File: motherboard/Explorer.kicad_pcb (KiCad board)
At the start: 2 copper layers, 80 x 55 mm, 73 parts, among them J1 USB_B, J2 EHZ, J3 EHN, J4 TTL_DEBUG, J5 MODE_SEL, J6 EHE, SW1 RESET, U1 ADS1262IPWR, U2 AMS1117-3.3, U4 locked

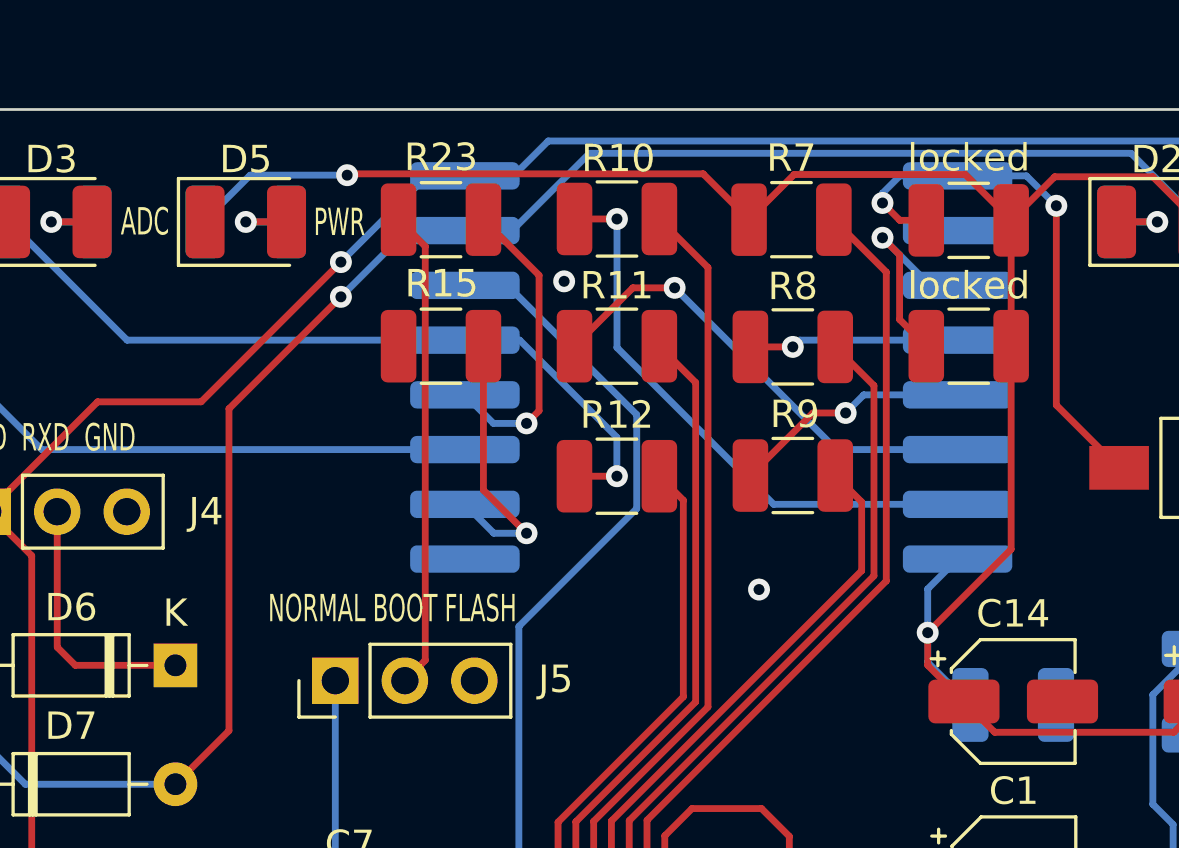
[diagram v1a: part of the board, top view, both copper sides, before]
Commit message: Update schematic & firmware
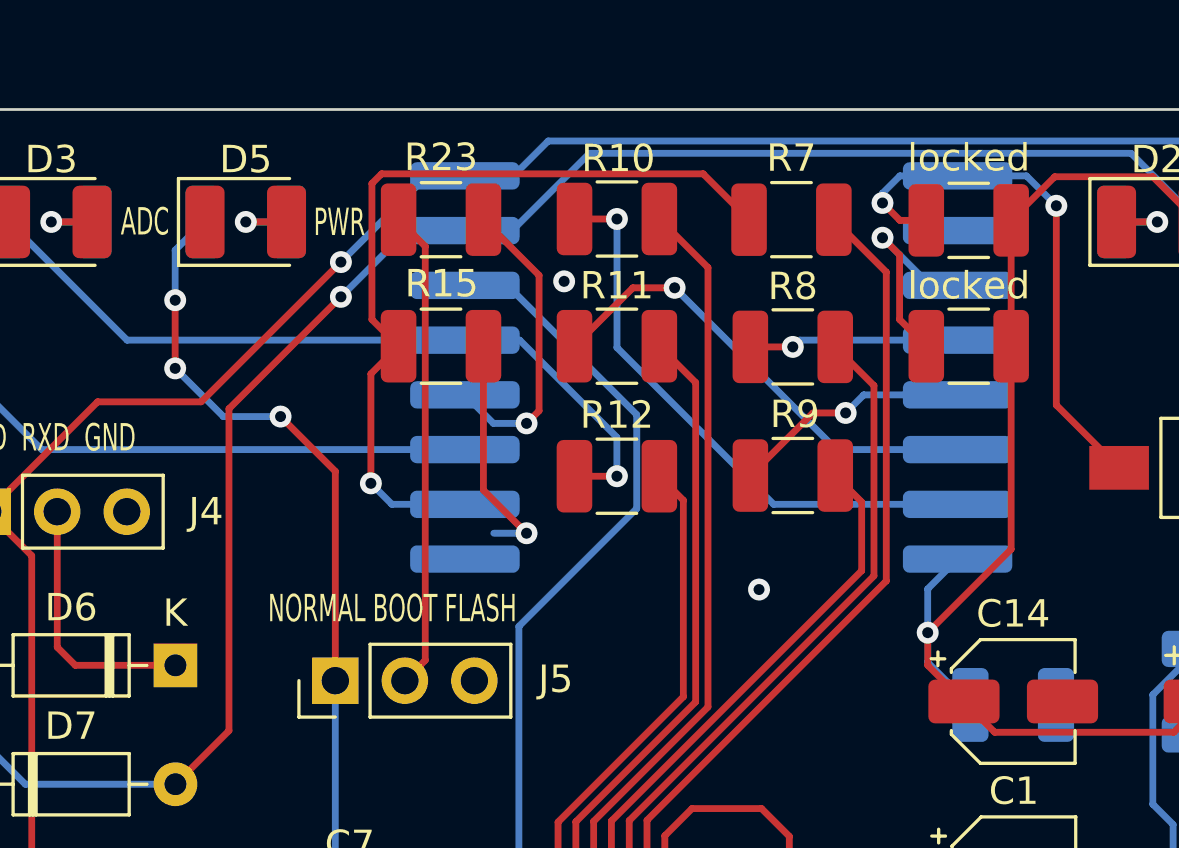
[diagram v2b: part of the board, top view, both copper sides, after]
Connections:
- R15 pad 1: Net-(U3-GPIO15) -> GND
- R15 pad 2: GND -> /ADC_START
- R7 pad 1: /+3.3v -> /ADC_START
- locked pad 10: Net-(U3-GPIO15) -> /ADC_START
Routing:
- net /ADC_START: track 0.00 -> 30.1 mm, vias 0 -> 1
- net /+3.3v: track 189.5 -> 178.0 mm, vias 6 -> 8
- net Net-(U3-GPIO15): track 10.2 -> 0.00 mm, vias 1 -> 0
- net GND: track 0.00 -> 8.68 mm, vias 5 -> 6
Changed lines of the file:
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@@
   (net 61 "Net-(U4-C2+)")
   (net 62 "Net-(U4-C2-)")
-  (net 63 "Net-(U3-GPIO15)")
+  (net 63 "/ADC_START")
   (net 64 "/MCU_MODE")
   (net 65 "Net-(U4-VS+)")
@@
       (stroke (width 0.1) (type solid)) (layer "F.Fab"))
     (pad "1" smd roundrect (at -1.55 0 180) (size 1.3 2.65) (layers "F.Cu" "F.Paste" "F.Mask") (roundrect_rratio 0.1923076923)
-      (net 63 "Net-(U3-GPIO15)") (pintype "passive"))
-    (pad "2" smd roundrect (at 1.55 0 180) (size 1.3 2.65) (layers "F.Cu" "F.Paste" "F.Mask") (roundrect_rratio 0.1923076923)
       (net 2 "GND") (pintype "passive"))
+    (pad "2" smd roundrect (at 1.55 0 180) (size 1.3 2.65) (layers "F.Cu" "F.Paste" "F.Mask") (roundrect_rratio 0.1923076923)
+      (net 63 "/ADC_START") (pintype "passive"))
     (model "${KICAD6_3DMODEL_DIR}/Resistor_SMD.3dshapes/R_1210_3225Metric.wrl"
       (offset (xyz 0 0 0))
@@
       (stroke (width 0.1) (type solid)) (layer "F.Fab"))
     (pad "1" smd roundrect (at -1.55 0) (size 1.3 2.65) (layers "F.Cu" "F.Paste" "F.Mask") (roundrect_rratio 0.1923076923)
-      (net 6 "/+3.3v") (pintype "passive"))
+      (net 63 "/ADC_START") (pintype "passive"))
     (pad "2" smd roundrect (at 1.55 0) (size 1.3 2.65) (layers "F.Cu" "F.Paste" "F.Mask") (roundrect_rratio 0.1923076923)
       (net 34 "Net-(U1-START)") (pintype "passive"))
@@
       (net 2 "GND") (pinfunction "GND") (pintype "power_in") (thermal_bridge_angle 45))
     (pad "10" smd roundrect (at 9 -8.5 180) (size 4 1) (layers "B.Cu" "B.Paste" "B.Mask") (roundrect_rratio 0.25)
-      (net 63 "Net-(U3-GPIO15)") (pinfunction "GPIO15") (pintype "bidirectional") (thermal_bridge_angle 45))
+      (net 63 "/ADC_START") (pinfunction "GPIO15") (pintype "bidirectional") (thermal_bridge_angle 45))
     (pad "11" smd roundrect (at 9 -6.5 180) (size 4 1) (layers "B.Cu" "B.Paste" "B.Mask") (roundrect_rratio 0.25)
       (net 46 "/MCU_STATE") (pinfunction "GPIO2") (pintype "bidirectional") (thermal_bridge_angle 45))
@@
   (segment (start 155.0416 95.631) (end 156.0576 96.647) (width 0.25) (layer "F.Cu") (net 1))
   (segment (start 156.0576 105.8418) (end 155.4076 105.8418) (width 0.25) (layer "F.Cu") (net 1))
+  (segment (start 144.8816 83.9978) (end 146.4564 85.5726) (width 0.25) (layer "F.Cu") (net 2))
+  (segment (start 144.8816 78.74) (end 144.8816 83.9978) (width 0.25) (layer "F.Cu") (net 2))
+  (via (at 146.4564 85.5726) (size 0.8) (drill 0.4) (layers "F.Cu" "B.Cu") (net 2))
   (via (at 154.95 87.63) (size 0.8) (drill 0.4) (layers "F.Cu" "B.Cu") (free) (net 2))
   (via (at 154.58 102.91) (size 0.8) (drill 0.4) (layers "F.Cu" "B.Cu") (free) (net 2))
@@
   (via (at 172.085 95.885) (size 0.8) (drill 0.4) (layers "F.Cu" "B.Cu") (free) (net 2))
   (via (at 147.83 76.37) (size 0.8) (drill 0.4) (layers "F.Cu" "B.Cu") (free) (net 2))
+  (segment (start 145.26 85.5726) (end 146.4564 85.5726) (width 0.25) (layer "B.Cu") (net 2))
   (segment (start 153.4576 100.1168) (end 153.4576 98.6374) (width 0.25) (layer "F.Cu") (net 3))
   (segment (start 153.4576 98.6374) (end 154.1526 97.9424) (width 0.25) (layer "F.Cu") (net 3))
@@
   (segment (start 164.1602 78.74) (end 164.1602 74.1426) (width 0.25) (layer "F.Cu") (net 6))
   (segment (start 165.7528 72.55) (end 169.3375 72.55) (width 0.25) (layer "F.Cu") (net 6))
-  (segment (start 154.5844 74.1172) (end 156.2344 72.4672) (width 0.25) (layer "F.Cu") (net 6))
   (segment (start 165.4844 101.7524) (end 162.4872 104.7496) (width 0.25) (layer "F.Cu") (net 6))
-  (segment (start 152.909 72.4418) (end 139.953 72.4418) (width 0.25) (layer "F.Cu") (net 6))
   (segment (start 151.8666 103.5812) (end 150.7998 103.5812) (width 0.25) (layer "F.Cu") (net 6))
   (segment (start 150.7998 103.5812) (end 150.2076 104.1734) (width 0.25) (layer "F.Cu") (net 6))
@@
   (segment (start 167.1828 101.7524) (end 165.4844 101.7524) (width 0.25) (layer "F.Cu") (net 6))
   (segment (start 172.5168 88.5444) (end 173.0502 88.5444) (width 0.25) (layer "F.Cu") (net 6))
-  (segment (start 162.4848 72.4672) (end 164.1602 74.1426) (width 0.25) (layer "F.Cu") (net 6))
+  (segment (start 139.4714 83.3114) (end 139.4714 90.9592) (width 0.25) (layer "F.Cu") (net 6))
   (segment (start 172.6375 72.55) (end 176.6375 72.55) (width 0.25) (layer "F.Cu") (net 6))
   (segment (start 128.9558 110.2106) (end 128.2954 109.5502) (width 0.25) (layer "F.Cu") (net 6))
-  (segment (start 156.2344 72.4672) (end 162.4848 72.4672) (width 0.25) (layer "F.Cu") (net 6))
-  (segment (start 139.953 72.4418) (end 139.9032 72.4916) (width 0.25) (layer "F.Cu") (net 6))
+  (segment (start 133.62 79.55) (end 133.62 77.06) (width 0.25) (layer "F.Cu") (net 6))
+  (segment (start 137.47 81.31) (end 139.4714 83.3114) (width 0.25) (layer "F.Cu") (net 6))
   (segment (start 164.1602 86.1568) (end 161.1122 89.2048) (width 0.25) (layer "F.Cu") (net 6))
   (segment (start 128.2954 109.5502) (end 127.0792 109.5502) (width 0.25) (layer "F.Cu") (net 6))
@@
   (segment (start 164.1602 78.74) (end 164.1602 86.1568) (width 0.25) (layer "F.Cu") (net 6))
   (segment (start 170.1062 92.8444) (end 163.5614 92.8444) (width 0.25) (layer "F.Cu") (net 6))
-  (segment (start 154.5844 74.1172) (end 152.909 72.4418) (width 0.25) (layer "F.Cu") (net 6))
   (segment (start 128.9558 110.9218) (end 128.9558 110.2106) (width 0.25) (layer "F.Cu") (net 6))
   (segment (start 171.2312 91.7194) (end 170.1062 92.8444) (width 0.25) (layer "F.Cu") (net 6))
-  (via (at 139.9032 72.4916) (size 0.8) (drill 0.4) (layers "F.Cu" "B.Cu") (net 6))
   (via (at 161.1122 89.2048) (size 0.8) (drill 0.4) (layers "F.Cu" "B.Cu") (net 6))
+  (via (at 133.62 77.06) (size 0.8) (drill 0.4) (layers "F.Cu" "B.Cu") (net 6))
+  (via (at 133.62 79.55) (size 0.8) (drill 0.4) (layers "F.Cu" "B.Cu") (net 6))
   (via (at 151.8666 103.5812) (size 0.8) (drill 0.4) (layers "F.Cu" "B.Cu") (net 6))
   (via (at 173.0502 88.5444) (size 0.8) (drill 0.4) (layers "F.Cu" "B.Cu") (net 6))
+  (via (at 137.47 81.31) (size 0.8) (drill 0.4) (layers "F.Cu" "B.Cu") (net 6))
   (via (at 128.9558 110.9218) (size 0.8) (drill 0.4) (layers "F.Cu" "B.Cu") (net 6))
   (via (at 167.1828 101.7524) (size 0.8) (drill 0.4) (layers "F.Cu" "B.Cu") (net 6))
@@
   (segment (start 138.9248 111.6468) (end 129.6808 111.6468) (width 0.25) (layer "B.Cu") (net 6))
   (segment (start 176.6862 100.4028) (end 176.6862 91.4747) (width 0.25) (layer "B.Cu") (net 6))
+  (segment (start 133.62 75.23) (end 133.62 77.06) (width 0.25) (layer "B.Cu") (net 6))
   (segment (start 175.0112 89.7997) (end 176.6862 91.4747) (width 0.25) (layer "B.Cu") (net 6))
   (segment (start 139.4714 97.689) (end 146.177 104.3946) (width 0.25) (layer "B.Cu") (net 6))
@@
   (segment (start 151.8666 103.5812) (end 150.7621 103.5812) (width 0.25) (layer "B.Cu") (net 6))
   (segment (start 168.2242 100.711) (end 170.078 100.711) (width 0.25) (layer "B.Cu") (net 6))
-  (segment (start 139.9032 72.4916) (end 136.3584 72.4916) (width 0.25) (layer "B.Cu") (net 6))
   (segment (start 146.177 104.3946) (end 138.9248 111.6468) (width 0.25) (layer "B.Cu") (net 6))
   (segment (start 170.078 100.711) (end 176.378 100.711) (width 0.25) (layer "B.Cu") (net 6))
+  (segment (start 137.47 81.31) (end 135.38 81.31) (width 0.25) (layer "B.Cu") (net 6))
   (segment (start 163.5406 105.3946) (end 167.1828 101.7524) (width 0.25) (layer "B.Cu") (net 6))
   (segment (start 161.1122 90.2847) (end 161.1122 89.2048) (width 0.25) (layer "B.Cu") (net 6))
-  (segment (start 136.3584 72.4916) (end 134.65 74.2) (width 0.25) (layer "B.Cu") (net 6))
   (segment (start 150.9237 105.3946) (end 163.5406 105.3946) (width 0.25) (layer "B.Cu") (net 6))
+  (segment (start 134.65 74.2) (end 133.62 75.23) (width 0.25) (layer "B.Cu") (net 6))
+  (segment (start 135.38 81.31) (end 133.62 79.55) (width 0.25) (layer "B.Cu") (net 6))
   (segment (start 173.7559 88.5444) (end 175.0112 89.7997) (width 0.25) (layer "B.Cu") (net 6))
   (segment (start 139.0396 101.7016) (end 140 101.7016) (width 0.25) (layer "F.Cu") (net 7))
@@
   (segment (start 134.7978 101.9048) (end 134.7978 101.2463) (width 0.25) (layer "B.Cu") (net 62))
   (segment (start 134.7978 101.2463) (end 133.7417 100.1902) (width 0.25) (layer "B.Cu") (net 62))
-  (segment (start 144.8816 83.9978) (end 146.4564 85.5726) (width 0.25) (layer "F.Cu") (net 63))
-  (segment (start 144.8816 78.74) (end 144.8816 83.9978) (width 0.25) (layer "F.Cu") (net 63))
-  (via (at 146.4564 85.5726) (size 0.8) (drill 0.4) (layers "F.Cu" "B.Cu") (net 63))
-  (segment (start 144.2044 84.517) (end 145.26 85.5726) (width 0.25) (layer "B.Cu") (net 63))
-  (segment (start 145.26 85.5726) (end 146.4564 85.5726) (width 0.25) (layer "B.Cu") (net 63))
+  (segment (start 140.8072 77.7656) (end 140.8072 72.7971) (width 0.25) (layer "F.Cu") (net 63))
+  (segment (start 141.1625 72.4418) (end 152.909 72.4418) (width 0.25) (layer "F.Cu") (net 63))
+  (segment (start 140.77 79.7516) (end 141.7816 78.74) (width 0.25) (layer "F.Cu") (net 63))
+  (segment (start 140.8072 72.7971) (end 141.1625 72.4418) (width 0.25) (layer "F.Cu") (net 63))
+  (segment (start 140.77 83.75) (end 140.77 79.7516) (width 0.25) (layer "F.Cu") (net 63))
+  (segment (start 141.7816 78.74) (end 140.8072 77.7656) (width 0.25) (layer "F.Cu") (net 63))
+  (segment (start 152.909 72.4418) (end 154.5844 74.1172) (width 0.25) (layer "F.Cu") (net 63))
+  (via (at 140.77 83.75) (size 0.8) (drill 0.4) (layers "F.Cu" "B.Cu") (net 63))
+  (segment (start 141.537 84.517) (end 144.2044 84.517) (width 0.25) (layer "B.Cu") (net 63))
+  (segment (start 140.77 83.75) (end 141.537 84.517) (width 0.25) (layer "B.Cu") (net 63))
   (segment (start 146.9136 76.1486) (end 144.8822 74.1172) (width 0.25) (layer "F.Cu") (net 64))
   (segment (start 146.4564 81.5594) (end 146.9136 81.1022) (width 0.25) (layer "F.Cu") (net 64))
